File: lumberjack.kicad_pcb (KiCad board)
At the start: 2 copper layers, 285.4 x 94.9 mm, 151 parts, among them J1 USB_OTG, J2 AVR_ISP_6, SW1 RESET, SW2 BOOT, U1 ATMEGA328-PU, Y1 16MHz

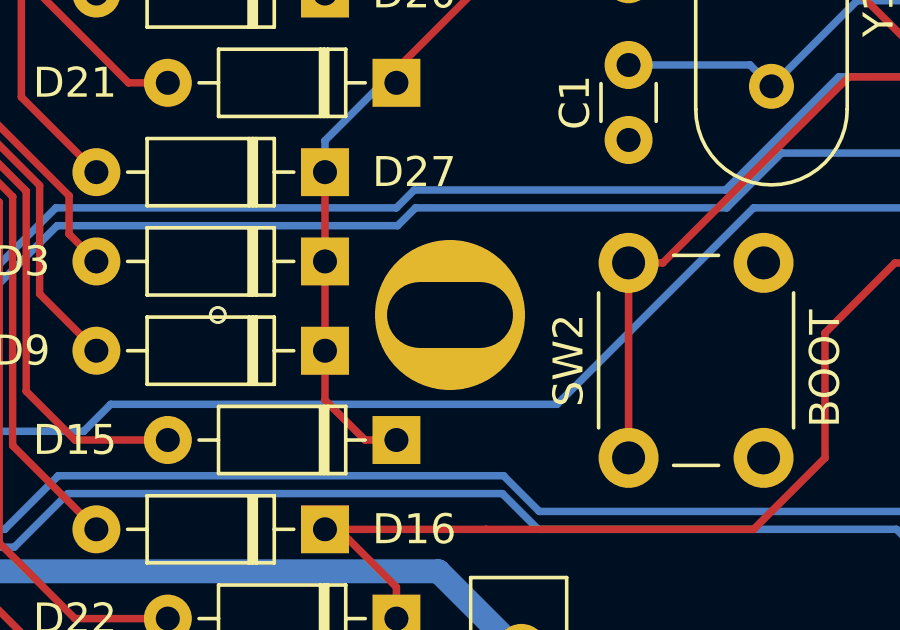
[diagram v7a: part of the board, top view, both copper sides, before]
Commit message: Rotate central mount hole 90 degrees
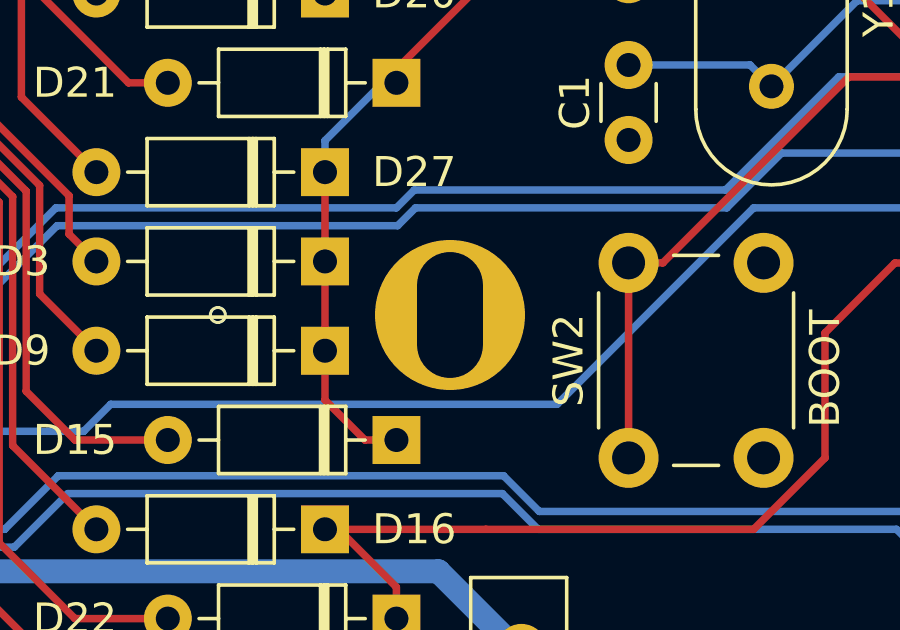
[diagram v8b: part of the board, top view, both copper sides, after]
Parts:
- turned H7 to 90 degrees
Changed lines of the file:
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@@
   )
   (module lumberjack:MountingSlot_M2 (layer F.Cu)
-    (at 138.112616 102.393836)
+    (at 138.112616 102.393836 90)
     (descr "Mounting Hole 2.2mm, no annular, M2")
     (tags "mounting hole 2.2mm no annular m2")
     (attr virtual)
-    (fp_text reference H7 (at 0 -3.2) (layer F.SilkS) hide
+    (fp_text reference H7 (at 0 -3.2 90) (layer F.SilkS) hide
       (effects (font (size 1 1) (thickness 0.15)))
     )
-    (fp_text value M2 (at 0 3.2) (layer F.Fab)
+    (fp_text value M2 (at 0 3.2 90) (layer F.Fab)
       (effects (font (size 1 1) (thickness 0.15)))
     )
     (fp_circle (center 0 0) (end 2.45 0) (layer F.CrtYd) (width 0.05))
     (fp_circle (center 0 0) (end 2.2 0) (layer Cmts.User) (width 0.15))
-    (fp_text user %R (at 0.3 0) (layer F.Fab)
+    (fp_text user %R (at 0.3 0 90) (layer F.Fab)
       (effects (font (size 1 1) (thickness 0.15)))
     )
-    (pad "" np_thru_hole circle (at 0 0) (size 5 5) (drill oval 4.2 2.2) (layers *.Cu *.Mask))
+    (pad "" np_thru_hole circle (at 0 0 90) (size 5 5) (drill oval 4.2 2.2) (layers *.Cu *.Mask))
   )
   (module lumberjack:MX (layer F.Cu)
@@
   (segment (start 145.207929 100.65634) (end 151.407961 94.456308) (width 0.25) (layer F.Cu) (net 14))
   (segment (start 144.065746 100.65634) (end 145.207929 100.65634) (width 0.25) (layer F.Cu) (net 14) (status 10))
-  (segment (start 151.069206 94.456308) (end 154.78138 94.456308) (width 0.25) (layer B.Cu) (net 14) (status 20))
-  (segment (start 136.326677 98.821958) (end 136.92199 98.226645) (width 0.25) (layer B.Cu) (net 14))
+  (segment (start 118.426193 105.370398) (end 124.974633 98.821958) (width 0.25) (layer B.Cu) (net 14))
   (segment (start 91.44008 99.853836) (end 91.44008 102.751027) (width 0.25) (layer B.Cu) (net 14) (status 10))
+  (segment (start 136.326677 98.821958) (end 136.92199 98.226645) (width 0.25) (layer B.Cu) (net 14))
+  (segment (start 147.298869 98.226645) (end 151.069206 94.456308) (width 0.25) (layer B.Cu) (net 14))
   (segment (start 91.44008 102.751027) (end 94.059451 105.370398) (width 0.25) (layer B.Cu) (net 14))
-  (segment (start 94.059451 105.370398) (end 118.426193 105.370398) (width 0.25) (layer B.Cu) (net 14))
-  (segment (start 118.426193 105.370398) (end 124.974633 98.821958) (width 0.25) (layer B.Cu) (net 14))
   (segment (start 124.974633 98.821958) (end 136.326677 98.821958) (width 0.25) (layer B.Cu) (net 14))
-  (segment (start 147.298869 98.226645) (end 151.069206 94.456308) (width 0.25) (layer B.Cu) (net 14))
   (segment (start 136.92199 98.226645) (end 147.298869 98.226645) (width 0.25) (layer B.Cu) (net 14))
+  (segment (start 94.059451 105.370398) (end 118.426193 105.370398) (width 0.25) (layer B.Cu) (net 14))
+  (segment (start 151.069206 94.456308) (end 154.78138 94.456308) (width 0.25) (layer B.Cu) (net 14) (status 20))
   (segment (start 15.239968 80.803772) (end 15.240016 80.80382) (width 0.25) (layer B.Cu) (net 15) (status 30))
   (segment (start 15.239968 61.75375) (end 15.239968 80.803772) (width 0.25) (layer B.Cu) (net 15) (status 30))
@@
   (segment (start 53.340048 99.853836) (end 53.340048 80.80382) (width 0.25) (layer B.Cu) (net 17) (status 30))
   (segment (start 53.340048 80.80382) (end 53.340048 61.753804) (width 0.25) (layer B.Cu) (net 17) (status 30))
-  (segment (start 75.459446 105.820409) (end 72.390064 102.751027) (width 0.25) (layer B.Cu) (net 17))
-  (segment (start 147.339966 98.821958) (end 136.963087 98.821958) (width 0.25) (layer B.Cu) (net 17))
   (segment (start 149.165616 96.996308) (end 147.339966 98.821958) (width 0.25) (layer B.Cu) (net 17))
-  (segment (start 72.390064 102.751027) (end 72.390064 99.853836) (width 0.25) (layer B.Cu) (net 17) (status 20))
-  (segment (start 154.78138 96.996308) (end 149.165616 96.996308) (width 0.25) (layer B.Cu) (net 17) (status 10))
+  (segment (start 75.459446 105.820409) (end 72.390064 102.751027) (width 0.25) (layer B.Cu) (net 17))
+  (segment (start 118.612592 105.820409) (end 75.459446 105.820409) (width 0.25) (layer B.Cu) (net 17))
   (segment (start 125.01573 99.417271) (end 118.612592 105.820409) (width 0.25) (layer B.Cu) (net 17))
   (segment (start 136.367774 99.417271) (end 125.01573 99.417271) (width 0.25) (layer B.Cu) (net 17))
+  (segment (start 72.390064 102.751027) (end 72.390064 99.853836) (width 0.25) (layer B.Cu) (net 17) (status 20))
   (segment (start 136.963087 98.821958) (end 136.367774 99.417271) (width 0.25) (layer B.Cu) (net 17))
-  (segment (start 118.612592 105.820409) (end 75.459446 105.820409) (width 0.25) (layer B.Cu) (net 17))
+  (segment (start 154.78138 96.996308) (end 149.165616 96.996308) (width 0.25) (layer B.Cu) (net 17) (status 10))
+  (segment (start 147.339966 98.821958) (end 136.963087 98.821958) (width 0.25) (layer B.Cu) (net 17))
   (segment (start 91.44008 61.753804) (end 110.490096 61.753804) (width 0.25) (layer F.Cu) (net 18) (status 30))
   (segment (start 110.490096 61.753804) (end 110.490096 80.80382) (width 0.25) (layer B.Cu) (net 18) (status 30))
